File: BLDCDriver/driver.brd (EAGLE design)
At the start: 61 parts, among them CON1 XT30PW-M, Q2 SIZ240DT-T1-GE3, Q3 SIZ240DT-T1-GE3, Q4 SIZ240DT-T1-GE3, U1 QFN50P400X400X100-25NDRV8300D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, U2 AS5048A-HTSP-500, U4 SOP80P620X125-8N

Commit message: CANに対応していき
# ==== Emojis ====
# ✨ :sparkles: Add new feature
# ✅  :white_check_mark: Update existing feature (not bug)
# ⚠️  :warning: Fix bug/error
# 🔥  :fire: Remove files or features
# ✏️ :pencil2: Fix typos
# 📝  :memo: Update documentation
# ♻️  :recycle: Dependencies update
# 🐧  :penguin: Improved the Linux
# 🍎  :apple: Improved the macOS
# 🔖 :bookmark: Add new library
# 🎉  :tada: Initial commit

# ==== Format ====
# :emoji: Subject
#
# Commit body...

# ==== Messages ====
# 新規(ファイル)機能追加: Add
# 機能修正、既存機能追加（バグではない): Update
# リファクタリング: Clean
# ファイル名変更:
# 削除など: Remove
# バグ修正: Fix
# バージョンアップ: Upgrade
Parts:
- moved R12 29.1 mm to (14.2, 1.79)
- moved R9 26.8 mm to (15.1, -0.79), turned to 90 degrees
- moved R15 9.36 mm to (21.1, 2.97)
- moved R17 5.81 mm to (21.9, 0.43), turned to 90 degrees
- moved U4 1.28 mm to (18.0, -2.09)
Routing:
- net N$10: track 12.7 -> 0.00 mm
- net U: track 9.92 -> 7.27 mm

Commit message: ちょっと希望が見えた
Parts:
- moved R8 48.7 mm to (-16.3, 8.30)
- moved R12 37.0 mm to (-19.5, 17.2)
- moved R15 37.0 mm to (-12.5, 18.4)
- moved R16 37.0 mm to (-15.9, 18.4)
- moved R17 37.0 mm to (-11.7, 15.8)
- moved R9 37.0 mm to (-18.6, 14.6)
- moved U4 37.0 mm to (-15.7, 13.3)
- moved U2 29.1 mm to (21.6, 29.4)
- moved CON1 28.2 mm to (13.5, 37.0)
- moved C15 27.7 mm to (-17.6, 39.4)
- moved C11 27.7 mm to (-17.6, 36.0)
- moved C34 27.7 mm to (-17.6, 41.2)
- moved C4 27.7 mm to (-17.5, 46.0)
- moved D1 27.7 mm to (-17.7, 26.1)
- moved D2 27.7 mm to (-13.3, 26.0)
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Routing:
- net U_CS: track 17.8 -> 0.00 mm
- net W: track 15.0 -> 0.00 mm
- net V_CS: track 12.6 -> 0.00 mm
- net U: track 7.27 -> 2.83 mm
- net LC: track 1.56 -> 0.00 mm
- net LB: track 1.53 -> 0.00 mm
- net HB: track 1.51 -> 0.00 mm
- net GND: track 1.43 -> 0.00 mm
- removed copper zone on layer 1, net GND
- removed copper zone on layer 1, net PVDD
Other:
- board outline added: 42 x 51 mm

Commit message: 希望が見えてきた
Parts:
- removed C18: (no value), cap-pan40:E3,5-8
- removed CON1: XT30PW-M, XTn0 amass:XT30PW-M
- added X2: JST-XH-06-PIN-LONG-PAD, Rembrandt Electronics - JST XH Connectors v1-0:JST-XH-06-PACKAGE-LONG-PAD
- moved D1 35.3 mm to (15.3, 38.6)
- moved R19 35.3 mm to (15.3, 37.2)
- moved D2 29.6 mm to (10.4, 43.8)
- moved R27 29.6 mm to (10.4, 42.4)
- moved R16 27.5 mm to (7.78, 32.4)
- moved R8 27.4 mm to (6.99, 22.9)
- moved U4 27.1 mm to (7.30, 27.6)
- moved R9 26.4 mm to (4.45, 27.6), turned to 270 degrees
- moved R15 26.0 mm to (11.7, 27.6), turned to 270 degrees
- moved C16 25.4 mm to (7.62, 36.4)
- moved C8 25.4 mm to (4.60, 36.4)
- moved C9 25.4 mm to (10.6, 36.4)
- moved R17 24.9 mm to (10.2, 27.6)
- moved R12 24.6 mm to (2.86, 27.6), turned to 90 degrees
- moved JP2 18.6 mm to (10.6, 48.9), flipped to the bottom
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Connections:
- new net CANH: X2.5
- new net CANL: X2.6
- net 5V: now also X2.4
- net GND: now also X2.3; no longer C18.-, CON1.-
- net GVDD_IN: now also X2.1
- net PVDD: now also X2.2; no longer C18.+, CON1.+
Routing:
- net PVDD: track 0.00 -> 9.99 mm
- net GND: track 0.00 -> 9.09 mm
- net GVDD_IN: track 0.00 -> 8.21 mm
- net N$9: track 0.00 -> 6.97 mm
- net N$11: track 0.00 -> 5.20 mm
- net C_V: track 0.00 -> 1.97 mm
- net N$8: track 0.00 -> 1.93 mm
- net N$10: track 0.00 -> 1.92 mm
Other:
- board text added: "+5V"
- board text added: "CANH"
- board text added: "CANL"
- board text added: "GND"
- board text added: "GVDD"
- board text added: "POWER"

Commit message: 配線頑張った
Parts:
- removed D7, D8: WHITE, SparkFun-LED:LED-0603
- removed R21, R22: 1k, Custom_Designed_By_Yusei:R0603
- added C10, C18: 0.1UF, Custom_Designed_By_Yusei:1608
- added REG: AP7333, SOT95P237X112-3N:SOT95P237X112-3N
- added U3: MCP2562-E/SN, MCP2562-E_SN:SOIC127P600X175-8N
- C13: value 0.1UF_1608 -> 0.1UF
- moved R23 55.8 mm to (41.4, 21.6), turned to 270 degrees
- moved D6 55.3 mm to (41.4, 24.8), turned to 90 degrees
- moved C11 54.0 mm to (35.2, 24.8)
- moved C15 42.1 mm to (22.9, 27.5)
- moved C12 38.3 mm to (20.6, 39.2), turned to 90 degrees
- moved C34 28.7 mm to (5.71, 24.3), turned to 90 degrees
- moved D3 27.5 mm to (12.9, 37.9)
- moved R20 26.8 mm to (12.9, 36.5), turned to 0 degrees
- moved C4 21.4 mm to (3.81, 44.0)
- moved D1 10.8 mm to (11.9, 48.9), turned to 90 degrees
- moved R19 9.33 mm to (11.9, 45.9), flipped to the bottom, turned to 90 degrees
- moved R16 9.02 mm to (11.7, 24.3), flipped to the bottom, turned to 90 degrees
- moved C13 8.53 mm to (38.4, 35.4), turned to 270 degrees
- moved R9 7.95 mm to (12.4, 27.1), turned to 180 degrees
- moved R15 6.96 mm to (8.57, 21.4), turned to 180 degrees
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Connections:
- net POWERLED_RESISTOR renamed L
- removed net LED1: D7.A
- removed net LED2: D8.A
- removed net N$12: D8.C, R21.1
- removed net N$13: D7.C, R22.1
- new net CANRX: U3.4
- new net CANTX: U3.1
- net 3V3: now also C10.1, REG.2, U3.5
- net 5V: now also C18.1, REG.1, U3.3
- net CANH: now also U3.7
- net CANL: now also U3.6
- net GND: now also C10.2, C18.2, REG.3, U3.2, U3.8; no longer R21.2, R22.2
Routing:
- net GND: track 9.09 -> 115.4 mm, vias 0 -> 6
- net PVDD: track 9.99 -> 86.8 mm, vias 0 -> 1
- net 3V3: track 0.00 -> 74.6 mm
- net INC: track 0.00 -> 29.7 mm, vias 0 -> 3
- net 5V: track 0.00 -> 27.8 mm
- net U: track 2.83 -> 24.6 mm, vias 0 -> 2
- net INB: track 0.00 -> 20.9 mm, vias 0 -> 2
- net GLA: track 0.00 -> 20.7 mm
- net BSTA: track 0.00 -> 18.6 mm, vias 0 -> 2
- net CLK: track 0.00 -> 18.4 mm, vias 0 -> 1
- net INA: track 0.00 -> 18.2 mm, vias 0 -> 2
- net N$8: track 1.93 -> 19.5 mm, vias 0 -> 2
- net MISO: track 0.00 -> 17.2 mm, vias 0 -> 1
- net GVDD: track 0.00 -> 16.9 mm, vias 0 -> 15
- net V: track 0.00 -> 16.2 mm
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- added copper zone on layer 1, net GND
- added copper zone on layer 16, net GND
- added copper zone on layer 1, net GVDD
- added copper zone on layer 16, net GVDD
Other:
- board text added: "VIN"
- board text removed: "POWER"

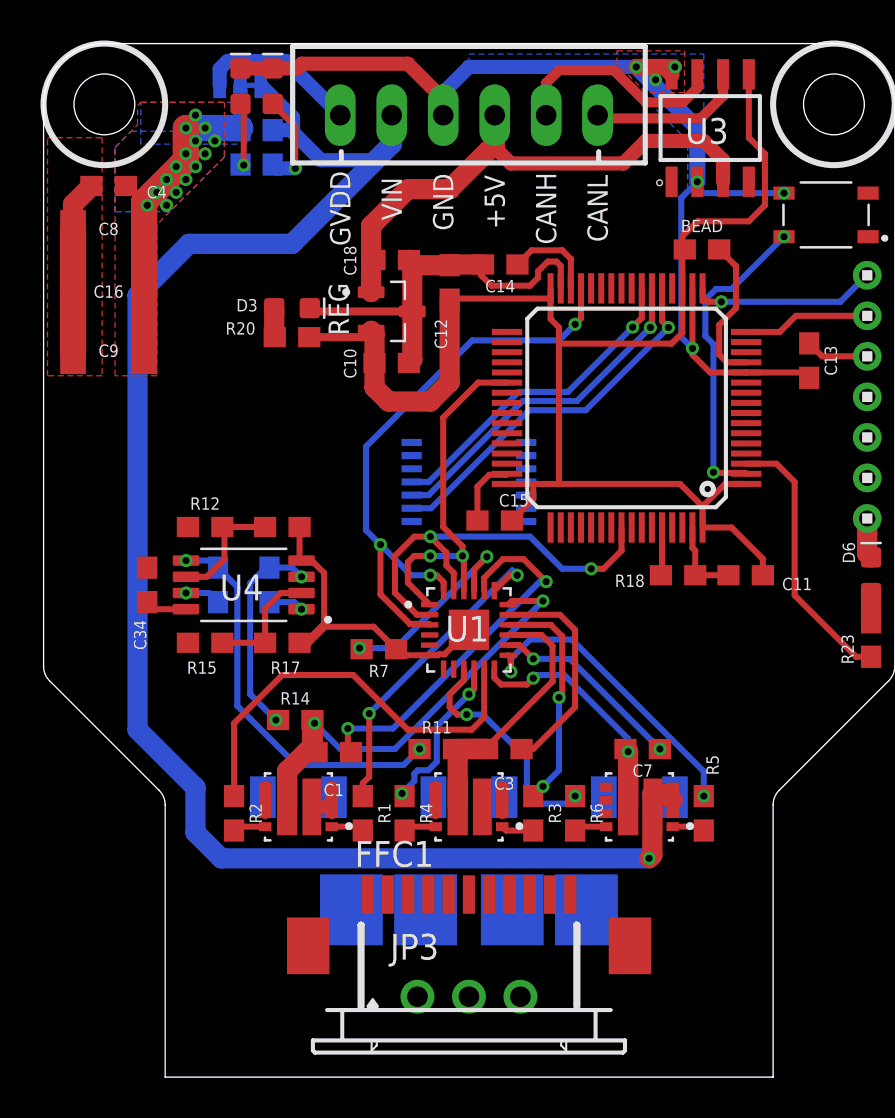
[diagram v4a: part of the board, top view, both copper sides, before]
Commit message: 𝐏𝐎𝐖𝐄𝐑した
# ==== Emojis ====
# ✨ :sparkles: Add new feature
# ✅  :white_check_mark: Update existing feature (not bug)
# ⚠️  :warning: Fix bug/error
# 🔥  :fire: Remove files or features
# ✏️ :pencil2: Fix typos
# 📝  :memo: Update documentation
# ♻️  :recycle: Dependencies update
# 🐧  :penguin: Improved the Linux
# 🍎  :apple: Improved the macOS
# 🔖 :bookmark: Add new library
# 🎉  :tada: Initial commit

# ==== Format ====
# :emoji: Subject
#
# Commit body...

# ==== Messages ====
# 新規(ファイル)機能追加: Add
# 機能修正、既存機能追加（バグではない): Update
# リファクタリング: Clean
# ファイル名変更:
# 削除など: Remove
# バグ修正: Fix
# バージョンアップ: Upgrade
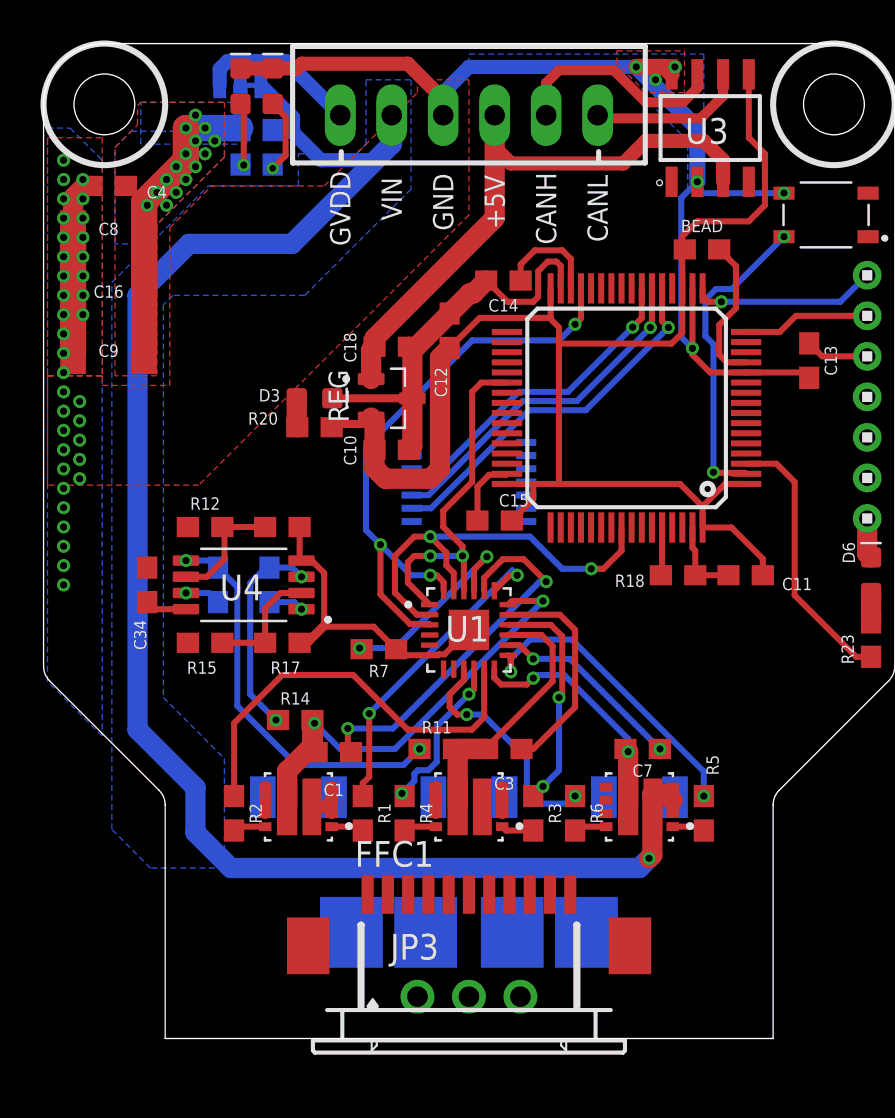
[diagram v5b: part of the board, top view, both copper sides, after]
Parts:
- moved R20 4.58 mm to (14.0, 32.1)
- moved D3 4.58 mm to (14.0, 33.5)
- moved C10 4.29 mm to (17.8, 31.0)
- moved C18 4.29 mm to (17.8, 36.0)
- moved REG 4.29 mm to (17.8, 33.5)
- moved C12 2.38 mm to (20.6, 36.8)
- moved R10 1.11 mm to (25.6, 7.14)
- moved R13 1.11 mm to (17.6, 7.14)
- moved C14 0.81 mm to (23.3, 39.3)
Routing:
- net 5V: track 27.8 -> 30.6 mm
- net N$14: track 4.82 -> 3.89 mm
- net GND: track 115.4 -> 116.2 mm, vias 6 -> 42
- net VCAP: track 4.55 -> 5.19 mm
- net 3V3: track 74.6 -> 75.1 mm
- added copper zone on layer 16, net PVDD
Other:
- board size 42 x 51 mm -> 42 x 49.1 mm

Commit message: FETにビア通した
# ==== Emojis ====
# ✨ :sparkles: Add new feature
# ✅  :white_check_mark: Update existing feature (not bug)
# ⚠️  :warning: Fix bug/error
# 🔥  :fire: Remove files or features
# ✏️ :pencil2: Fix typos
# 📝  :memo: Update documentation
# ♻️  :recycle: Dependencies update
# 🐧  :penguin: Improved the Linux
# 🍎  :apple: Improved the macOS
# 🔖 :bookmark: Add new library
# 🎉  :tada: Initial commit

# ==== Format ====
# :emoji: Subject
#
# Commit body...

# ==== Messages ====
# 新規(ファイル)機能追加: Add
# 機能修正、既存機能追加（バグではない): Update
# リファクタリング: Clean
# ファイル名変更:
# 削除など: Remove
# バグ修正: Fix
# バージョンアップ: Upgrade
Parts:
- removed C13: 0.1UF, Custom_Designed_By_Yusei:1608
- added R21: 10k, Custom_Designed_By_Yusei:R0603
- moved D3 3.50 mm to (16.7, 35.7), turned to 90 degrees
- moved C15 3.05 mm to (25.9, 27.9)
- moved R20 2.77 mm to (16.7, 32.7), turned to 270 degrees
- moved C14 2.51 mm to (25.7, 40.1)
- moved C12 2.51 mm to (23.0, 36.0)
- moved NUCLEO_MAIN 2.51 mm to (31.8, 33.8)
- moved C10 2.51 mm to (20.2, 31.8)
- moved C18 2.51 mm to (20.2, 36.8)
- moved REG 2.51 mm to (20.2, 34.3)
- moved R12 2.48 mm to (10.5, 28.7)
- moved R15 2.48 mm to (10.5, 23.0)
- moved R17 2.48 mm to (14.3, 23.0)
- moved R9 2.48 mm to (14.3, 28.7)
- moved R8 2.48 mm to (11.1, 25.9)
- moved U4 2.48 mm to (12.4, 25.9)
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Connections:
- net 3V3: now also R21.1
- net GND: no longer C13.2
- net NRST: now also R21.2; no longer C13.1
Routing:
- net W: track 12.2 -> 18.7 mm
- net PVDD: track 87.2 -> 91.1 mm, vias 1 -> 13
- net GND: track 116.2 -> 118.9 mm, vias 42 -> 54
- net USBRX: track 9.16 -> 6.45 mm
- net USBTX: track 6.30 -> 3.59 mm
- net MOSI: track 16.2 -> 18.9 mm
- net MISO: track 17.2 -> 19.9 mm
- net CLK: track 18.4 -> 21.1 mm
- net SW: track 15.5 -> 18.2 mm
- net INB: track 20.9 -> 23.4 mm
- net BOOT0: track 2.38 -> 4.25 mm
- net N$8: track 19.5 -> 21.3 mm
- net 5V: track 30.6 -> 28.9 mm
- net 3V3: track 75.1 -> 76.8 mm, vias 0 -> 1
- net INC: track 29.7 -> 31.3 mm
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- added copper zone on layer 1, net PVDD
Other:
- board text added: "3V3"
- board text added: "RST"
- board text added: "RX"
- board text added: "SWCLK"
- board text added: "SWDIO"
- board text added: "TX"

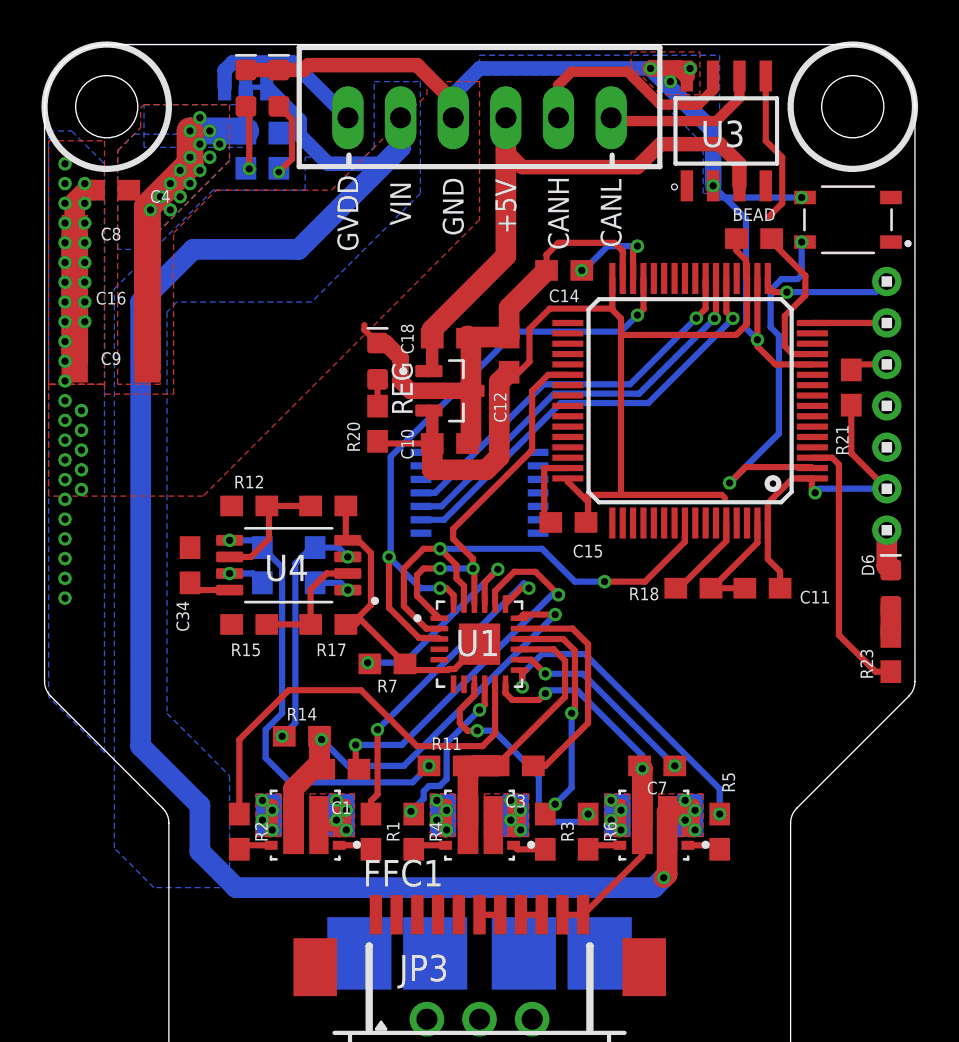
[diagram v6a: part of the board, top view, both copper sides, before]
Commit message: 配線1からやり直し
# ==== Emojis ====
# ✨ :sparkles: Add new feature
# ✅  :white_check_mark: Update existing feature (not bug)
# ⚠️  :warning: Fix bug/error
# 🔥  :fire: Remove files or features
# ✏️ :pencil2: Fix typos
# 📝  :memo: Update documentation
# ♻️  :recycle: Dependencies update
# 🐧  :penguin: Improved the Linux
# 🍎  :apple: Improved the macOS
# 🔖 :bookmark: Add new library
# 🎉  :tada: Initial commit

# ==== Format ====
# :emoji: Subject
#
# Commit body...

# ==== Messages ====
# 新規(ファイル)機能追加: Add
# 機能修正、既存機能追加（バグではない): Update
# リファクタリング: Clean
# ファイル名変更:
# 削除など: Remove
# バグ修正: Fix
# バージョンアップ: Upgrade
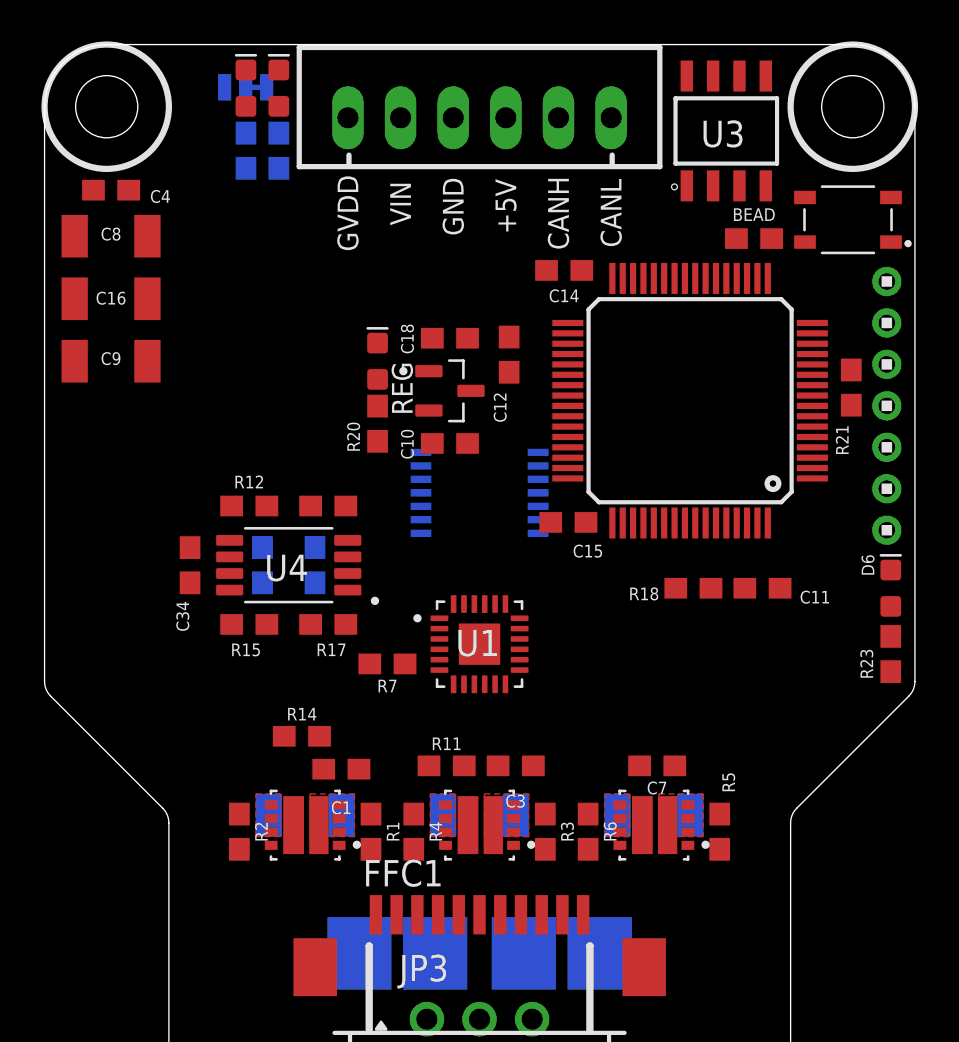
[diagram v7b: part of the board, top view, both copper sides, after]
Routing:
- net GND: track 118.9 -> 0.00 mm, vias 54 -> 0
- net PVDD: track 91.1 -> 0.00 mm, vias 13 -> 0
- net 3V3: track 76.8 -> 0.00 mm, vias 1 -> 0
- net INC: track 31.3 -> 0.00 mm, vias 3 -> 0
- net 5V: track 28.9 -> 0.00 mm
- net U: track 24.6 -> 0.00 mm, vias 2 -> 0
- net INB: track 23.4 -> 0.00 mm, vias 2 -> 0
- net N$8: track 21.3 -> 0.00 mm, vias 2 -> 0
- net CLK: track 21.1 -> 0.00 mm, vias 1 -> 0
- net GLA: track 20.7 -> 0.00 mm
- net MISO: track 19.9 -> 0.00 mm, vias 1 -> 0
- net INA: track 19.7 -> 0.00 mm, vias 2 -> 0
- net MOSI: track 18.9 -> 0.00 mm, vias 1 -> 0
- net W: track 18.7 -> 0.00 mm, vias 2 -> 0
- net BSTA: track 18.6 -> 0.00 mm, vias 2 -> 0
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- removed copper zone on layer 16, net GND
- removed copper zone on layer 1, net GVDD
- removed copper zone on layer 16, net GVDD
- removed copper zone on layer 16, net PVDD
